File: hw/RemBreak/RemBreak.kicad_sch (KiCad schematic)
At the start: 4 parts, among them J1 Screw_Terminal_01x04, J2 Screw_Terminal_01x04

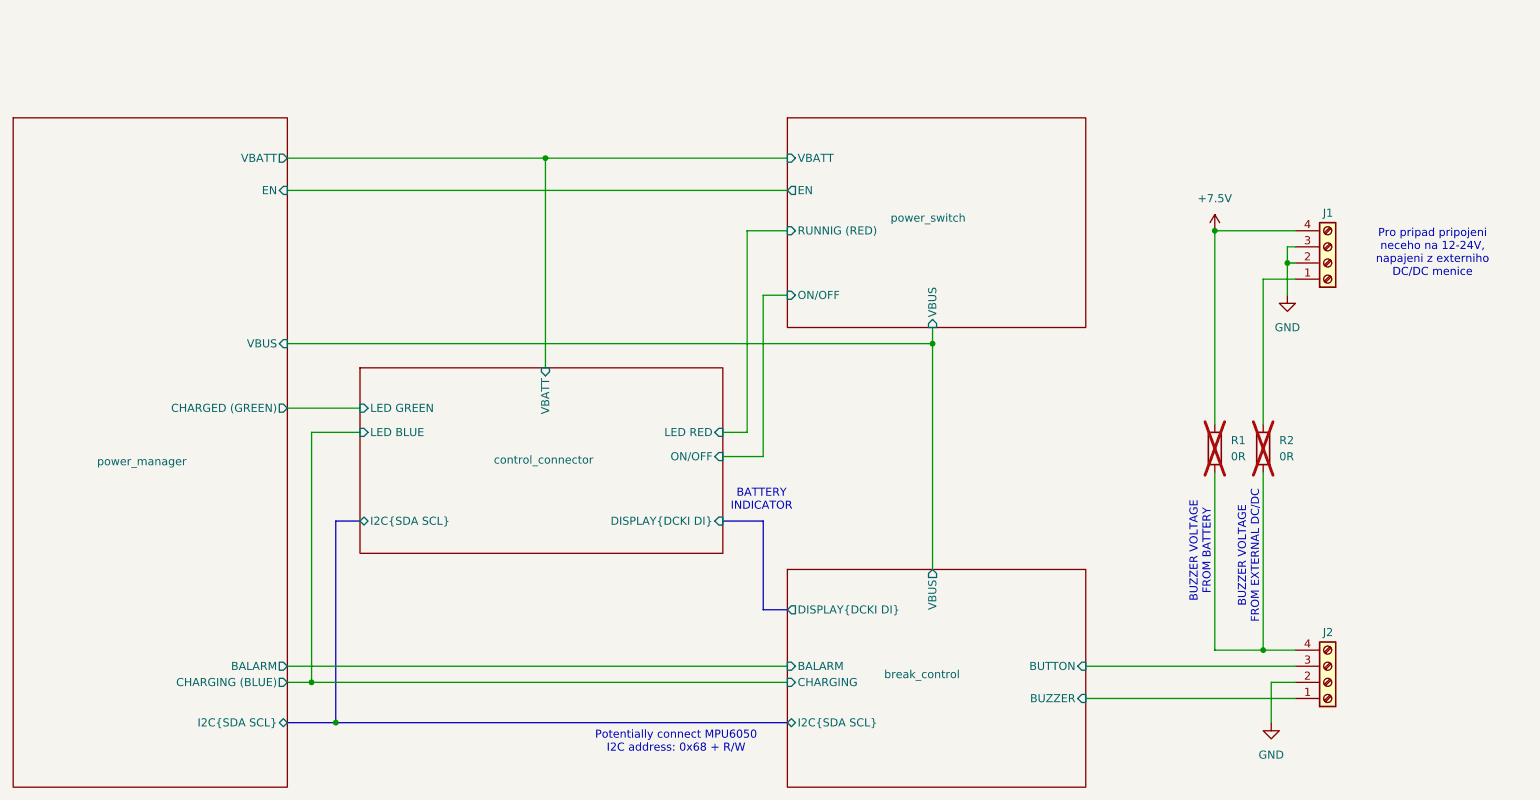
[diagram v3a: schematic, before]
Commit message: Note fonts changed to bold and added titles of the sheets included rev number
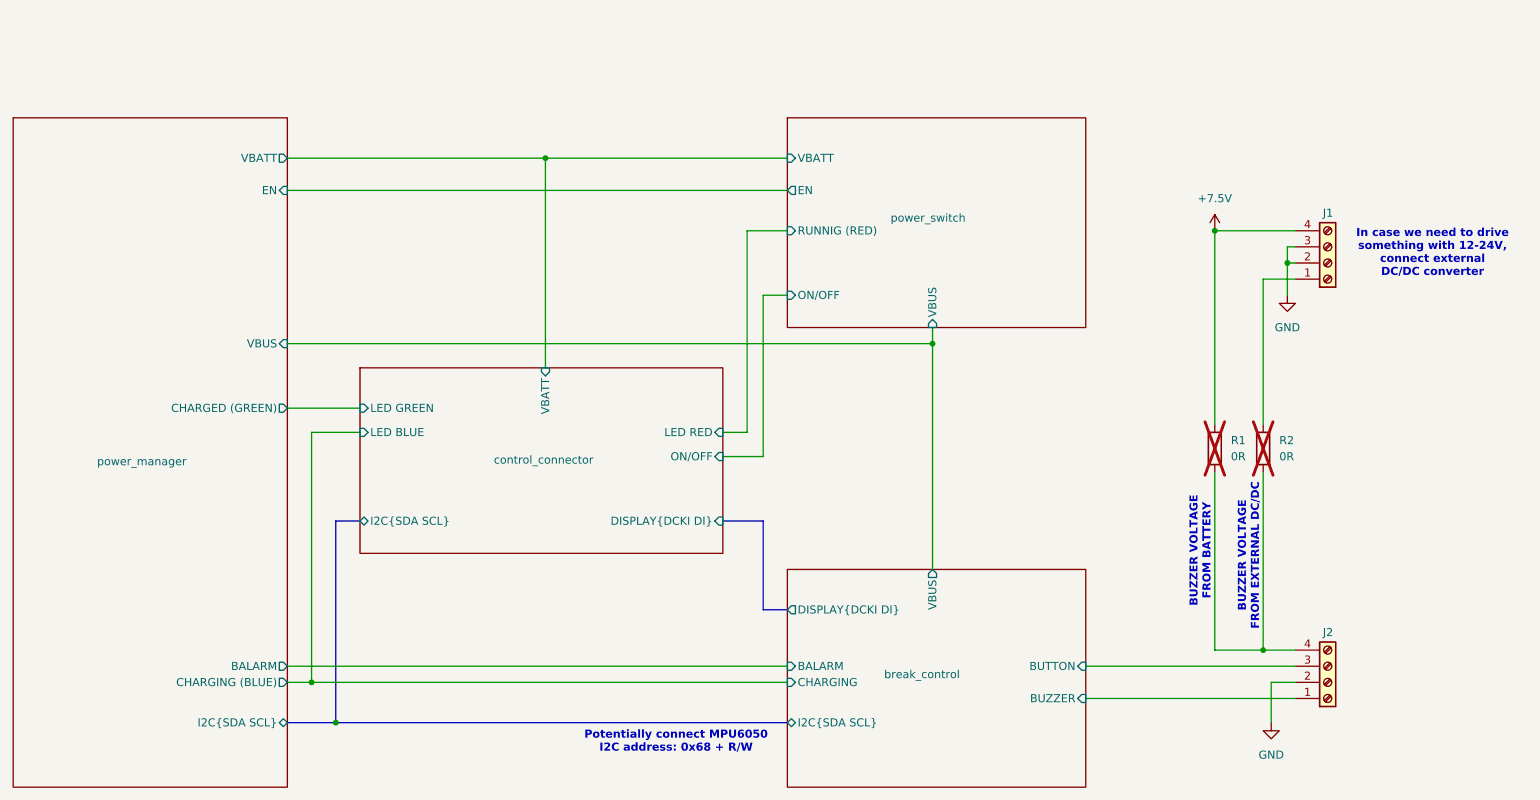
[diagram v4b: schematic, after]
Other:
- note added: "In case we need to drive something with 12-24V, connect external DC/DC converter"
- note removed: "BATTERY INDICATOR"
- note removed: "Pro pripad pripojeni neceho na 12-24V, napajeni z externiho DC/DC menice"
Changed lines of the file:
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@@
 	(title_block
 		(title "Remote Break Main Board")
-		(date "2024-10-28")
+		(date "2024-12-15")
+		(rev "1.0")
 	)
 	(bus_alias "I2C"
@@
 			(font
 				(size 1.27 1.27)
-			)
-		)
-	)
-	(text "BATTERY \nINDICATOR\n"
-		(exclude_from_sim no)
-		(at 157.226 103.378 0)
-		(effects
-			(font
-				(size 1.27 1.27)
+				(thickness 0.254)
+				(bold yes)
 			)
 		)
@@
 			(font
 				(size 1.27 1.27)
+				(thickness 0.254)
+				(bold yes)
 			)
 		)
@@
 			(font
 				(size 1.27 1.27)
+				(thickness 0.254)
+				(bold yes)
 			)
 		)
 	)
-	(text "Pro pripad pripojeni\nneceho na 12-24V,\nnapajeni z externiho \nDC/DC menice"
+	(text "In case we need to drive \nsomething with 12-24V, \nconnect external \nDC/DC converter"
 		(exclude_from_sim no)
 		(at 262.89 64.516 0)
@@
 			(font
 				(size 1.27 1.27)
+				(thickness 0.254)
+				(bold yes)
 			)
 		)

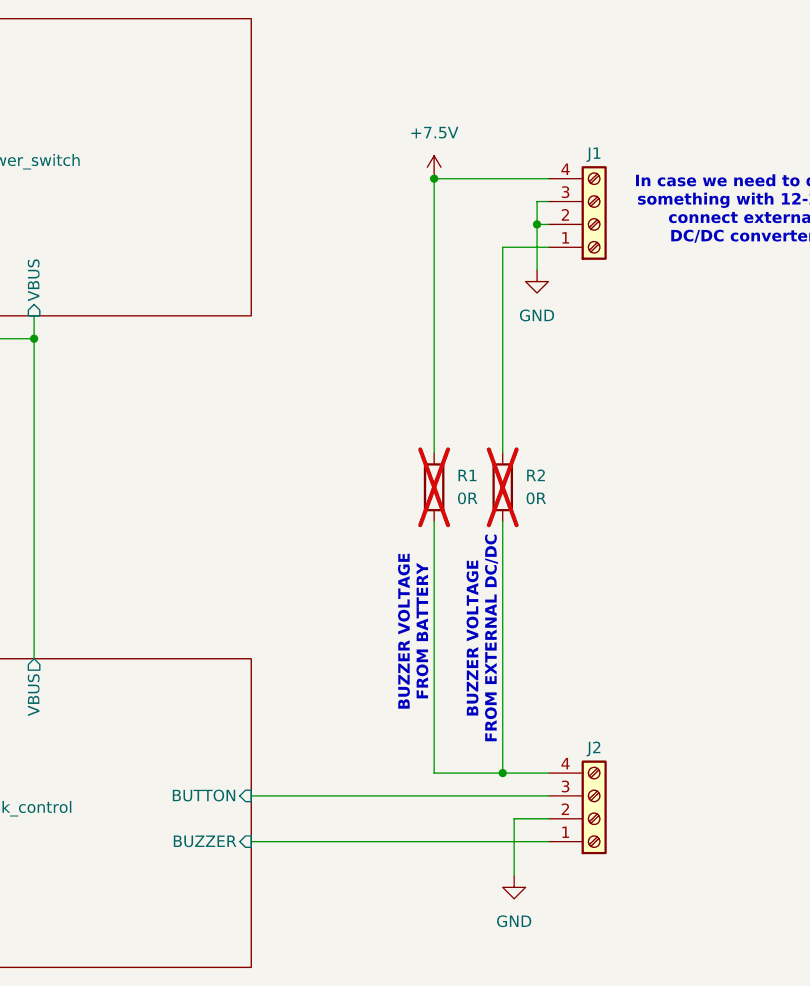
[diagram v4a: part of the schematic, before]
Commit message: first version and added jumper to connect buzz internally not just through handlebars
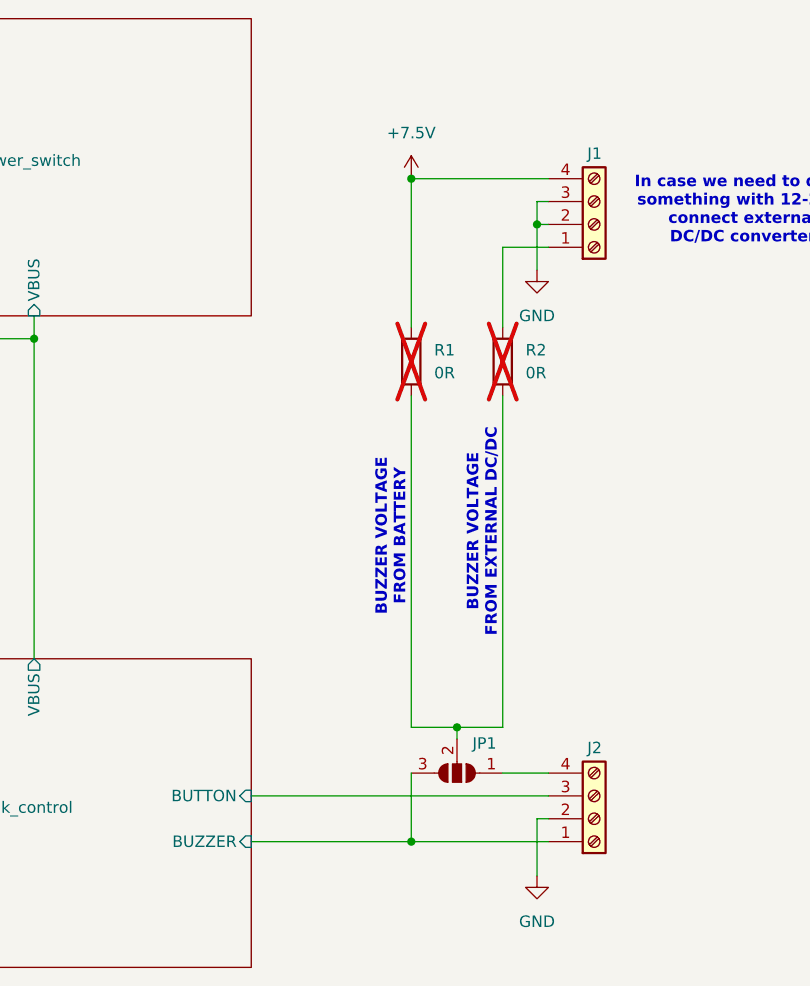
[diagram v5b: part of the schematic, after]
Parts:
- added JP1: SolderJumper_3_Open, Jumper:SolderJumper-3_P1.3mm_Open_RoundedPad1.0x1.5mm, symbol Jumper:SolderJumper_3_Open
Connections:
- net break_control/BUZZER: now also JP1.3 (B)
- net at R1.2, R2.2: now also JP1.2 (C); no longer J2.4 (Pin_4)
- new net: J2.4 (Pin_4), JP1.1 (A)
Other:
- moved on the sheet: R1, R2

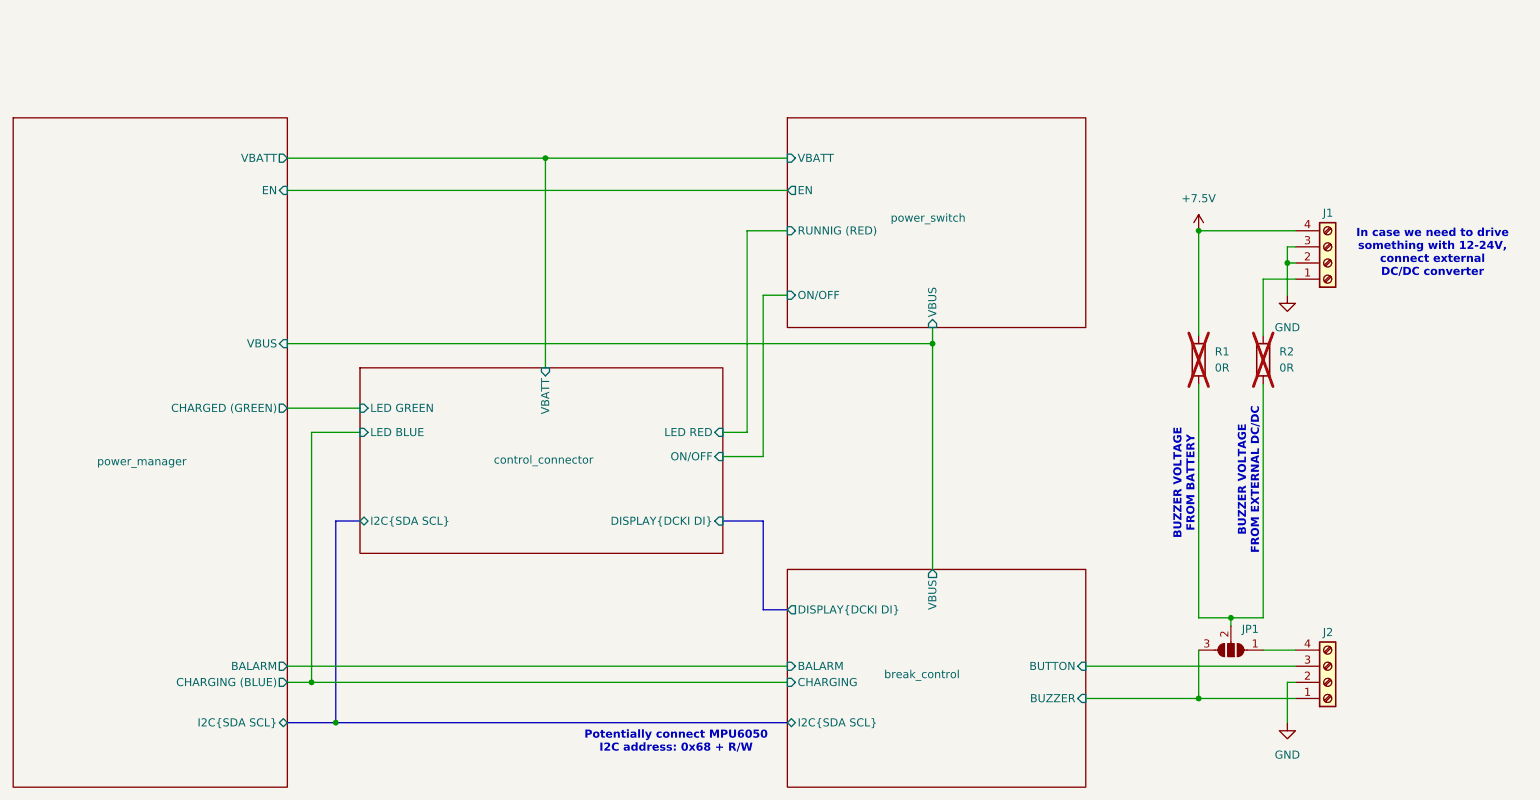
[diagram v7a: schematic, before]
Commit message: redrawing the schematics according the notes from the module design
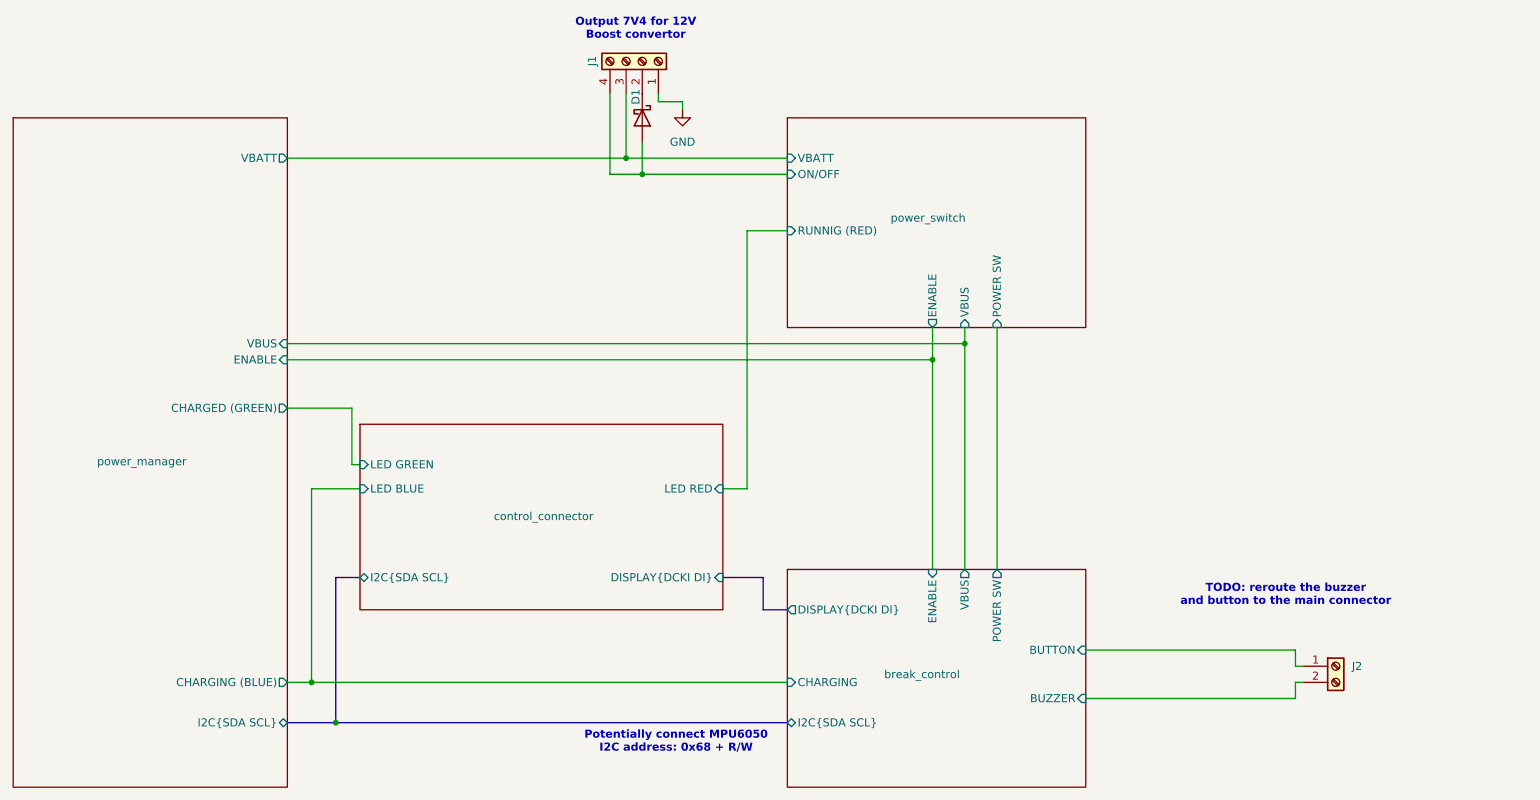
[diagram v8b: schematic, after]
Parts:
- removed J2: Screw_Terminal_01x04, TerminalBlock_Phoenix:TerminalBlock_Phoenix_MPT-0,5-4-2.54_1x04_P2.54mm_Horizontal, symbol Connector:Screw_Terminal_01x04
- removed JP1: SolderJumper_3_Open, Jumper:SolderJumper-3_P1.3mm_Open_RoundedPad1.0x1.5mm, symbol Jumper:SolderJumper_3_Open
- removed R1, R2: 0R, Resistor_SMD:R_0805_2012Metric_Pad1.20x1.40mm_HandSolder, symbol Device:R
- added D1: D_Schottky, symbol Device:D_Schottky
- added J2: Screw_Terminal_01x02, symbol Connector:Screw_Terminal_01x02
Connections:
- net GND: now also J1.1 (Pin_1); no longer J1.2 (Pin_2), J1.3 (Pin_3)
- net break_control/BUTTON: now also J2.1 (Pin_1)
- net break_control/BUZZER: now also J2.2 (Pin_2)
- net +7.5V renamed power_switch/ON/OFF
- net power_switch/ON/OFF: now also D1.2 (A)
- new net: D1.1 (K), J1.2 (Pin_2)
- new net power_manager/VBATT: J1.3 (Pin_3)
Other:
- sheet break_control ports: added ENABLE, POWER SW; removed BALARM
- sheet control_connector ports: added none; removed ON/OFF, VBATT
- sheet power_manager ports: added ENABLE; removed BALARM, EN
- sheet power_switch ports: added ENABLE, POWER SW; removed EN
- note added: "Output 7V4 for 12V Boost convertor"
- note added: "TODO: reroute the buzzer and button to the main connector"
- note removed: "BUZZER VOLTAGE FROM BATTERY"
- note removed: "BUZZER VOLTAGE FROM EXTERNAL DC/DC"
- note removed: "In case we need to drive something with 12-24V, connect external DC/DC converter"
- moved on the sheet: J1
